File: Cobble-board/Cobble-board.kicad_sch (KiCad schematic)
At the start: 5 parts

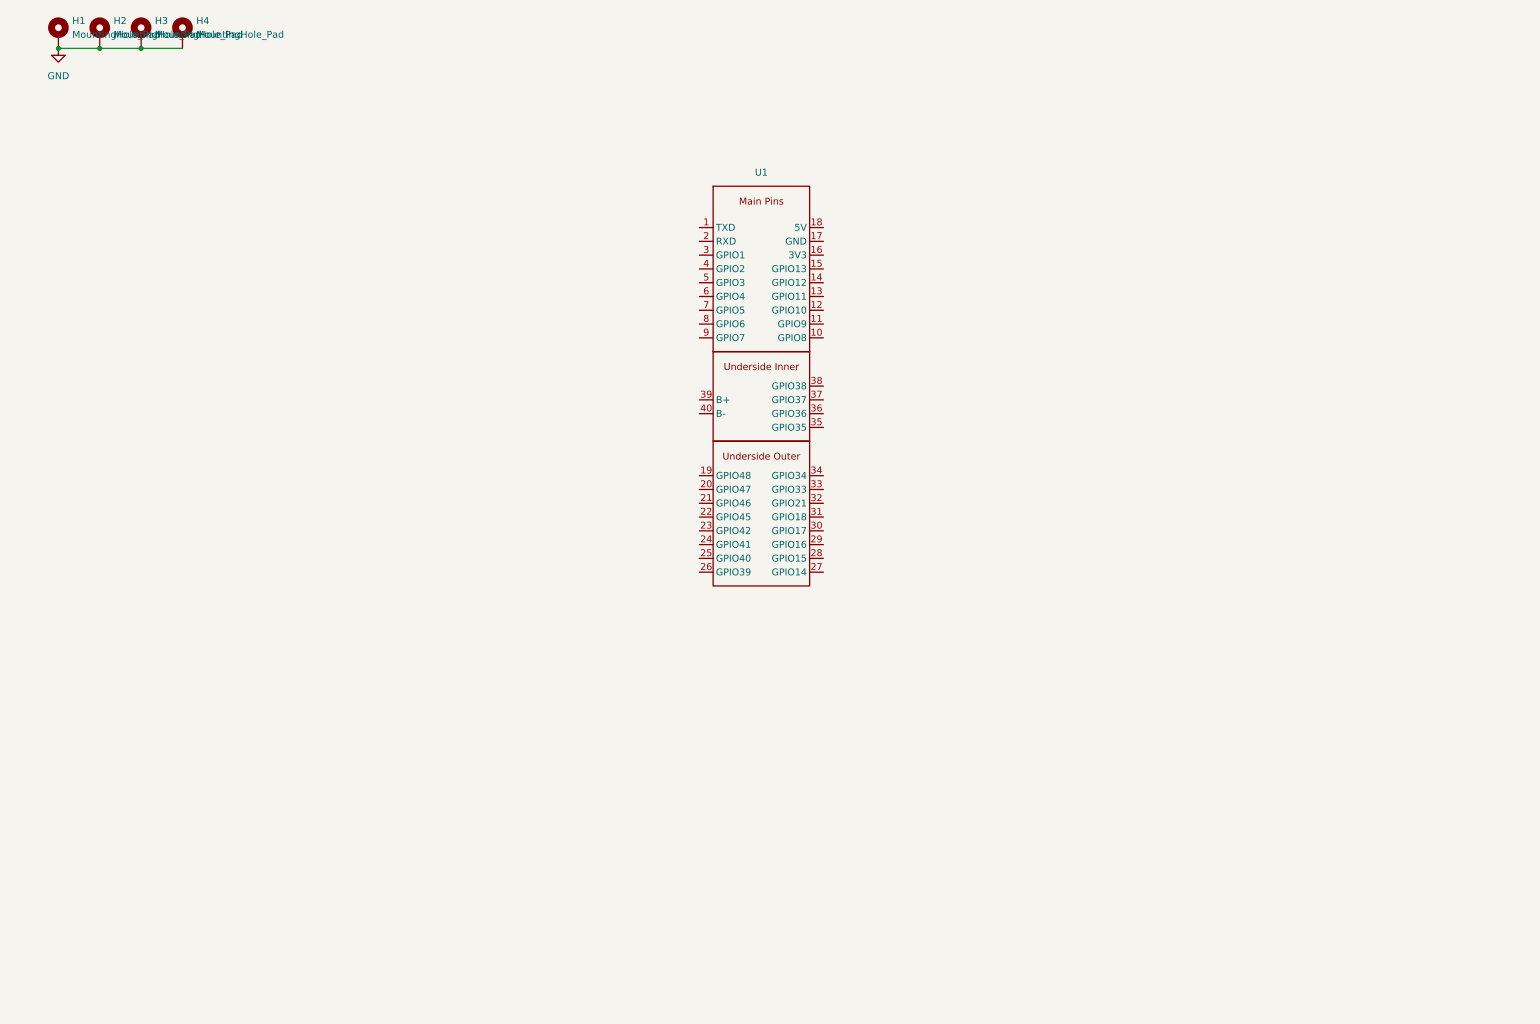
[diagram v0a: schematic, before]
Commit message: added most components.  waiting on clarification for speaker and i2c connectors
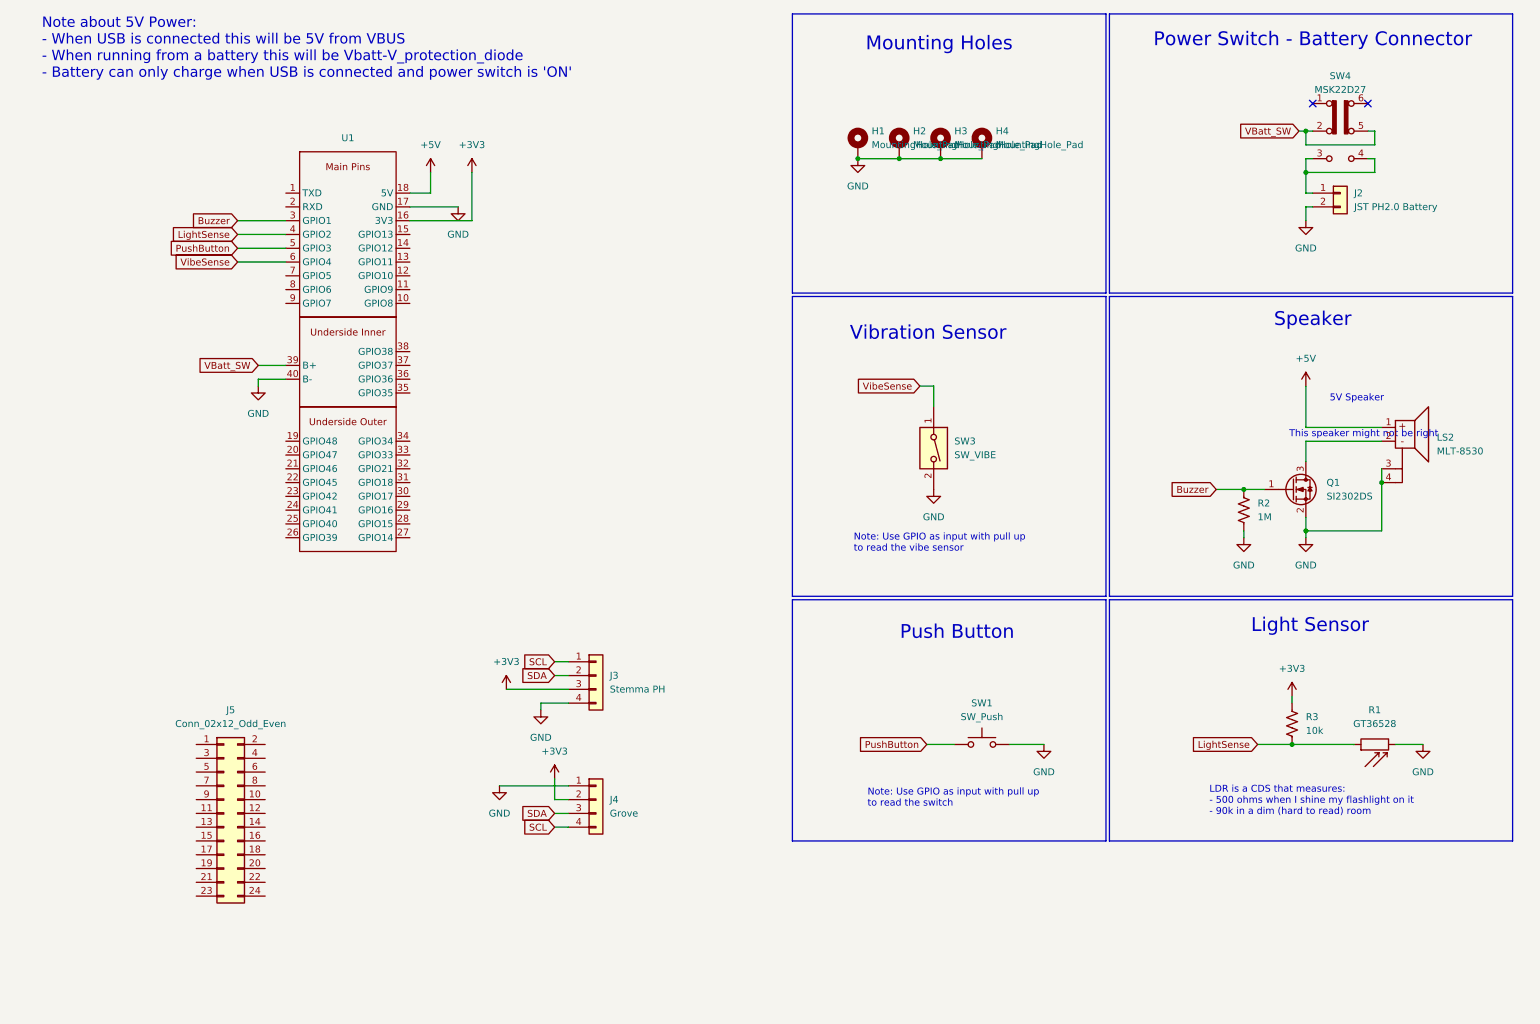
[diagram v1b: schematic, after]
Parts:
- added J2: JST PH2.0 Battery, Connector_JST:JST_PH_S2B-PH-K_1x02_P2.00mm_Horizontal, symbol Connector_Generic:Conn_01x02
- added J3: Stemma PH, Connector_JST:JST_PH_S4B-PH-K_1x04_P2.00mm_Horizontal, symbol Connector_Generic:Conn_01x04
- added J4: Grove, Connector_JST:JST_PH_S4B-PH-K_1x04_P2.00mm_Horizontal, symbol Connector_Generic:Conn_01x04
- added J5: Conn_02x12_Odd_Even, Connector_PinHeader_2.54mm:PinHeader_2x12_P2.54mm_Vertical_SMD, symbol Connector_Generic:Conn_02x12_Odd_Even
- added LS2: MLT-8530, Cobble_Library:MLT-8530, symbol Cobble_Library:MLT-8530
- added Q1: SI2302DS, Package_TO_SOT_SMD:SOT-23_Handsoldering, symbol Transistor_FET:Q_NMOS_GSD
- added R1: GT36528, Cobble_Library:GT36528, symbol Sensor_Optical:A1050
- added R2: 1M, Resistor_SMD:R_0603_1608Metric_Pad0.98x0.95mm_HandSolder, symbol Device:R_US
- added R3: 10k, Resistor_SMD:R_0603_1608Metric_Pad0.98x0.95mm_HandSolder, symbol Device:R_US
- added SW1: SW_Push, Button_Switch_SMD:SW_Push_1P1T_NO_CK_KSC6xxG, symbol Switch:SW_Push
- added SW3: SW_VIBE, Cobble_Library:X160, symbol Switch:SW_DIP_x01
- added SW4: MSK22D27, Cobble_Library:MSK22D27, symbol Switch:SW_Slide_DPDT
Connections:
- net GND: now also U1.17 (GND), U1.40 (B-), J2.2 (Pin_2), J3.4 (Pin_4), J4.1 (Pin_1), LS2.3 (Dummy), LS2.4 (Dummy), Q1.2 (S), R1.2, R2.2, SW1.2, SW3.2
- net +3V3: now reaches U1.16 (3V3)
- net +3V3: now also J3.3 (Pin_3), J4.2 (Pin_2), R3.1
- net +5V: now reaches U1.18 (5V)
- net +5V: now also LS2.1
- net Buzzer: now reaches U1.3 (GPIO1)
- net Buzzer: now also Q1.1 (G), R2.1
- net VBatt_SW: now reaches U1.39 (B+)
- net VBatt_SW: now also SW4.2 (B), SW4.5 (B)
- net LightSense: now reaches U1.4 (GPIO2)
- net LightSense: now also R1.1, R3.2
- net PushButton: now reaches U1.5 (GPIO3)
- net PushButton: now also SW1.1
- net VibeSense: now reaches U1.6 (GPIO4)
- net VibeSense: now also SW3.1
- new net: J2.1 (Pin_1), SW4.3 (C), SW4.4 (A)
- new net: LS2.2, Q1.3 (D)
- new net SCL: J3.1 (Pin_1), J4.4 (Pin_4)
- new net SDA: J3.2 (Pin_2), J4.3 (Pin_3)
- no-connect marks 0 -> 2
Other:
- note added: "5V Speaker"
- note added: "LDR is a CDS that measures: - 500 ohms when I shine my flashlight on it - 90k in a dim (hard to read) room"
- note added: "Light Sensor"
- note added: "Mounting Holes"
- note added: "Note about 5V Power: - When USB is connected this will be 5V from VBUS - When running from a battery this will be Vbatt-V_protection_diode - Battery can only charge when USB is connected and power switch is 'ON'"
- note added: "Note: Use GPIO as input with pull up to read the switch"
- note added: "Note: Use GPIO as input with pull up to read the vibe sensor"
- note added: "Power Switch - Battery Connector"
- note added: "Push Button"
- note added: "Speaker"
- note added: "This speaker might not be right"
- note added: "Vibration Sensor"
- moved on the sheet: H1, H2, H3, H4, U1

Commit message: main PWB is nearly complete.  need to add logo and fix one rat line.  added a cobble-board-test for a simpler single sided fab test board
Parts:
- J2: footprint Connector_JST:JST_PH_S2B-PH-K_1x02_P2.00mm_Horizontal -> Cobble_Library:Battery_1x02_P2.00mm_Horizontal
- J3, J4: footprint Connector_JST:JST_PH_S4B-PH-K_1x04_P2.00mm_Horizontal -> Cobble_Library:Stemma_Grove_1x04_P2.00mm_Horizontal
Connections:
- net +3V3: now also J5.10 (Pin_10), J5.15 (Pin_15), J5.16 (Pin_16), J5.21 (Pin_21), J5.4 (Pin_4), J5.9 (Pin_9)
- net +5V: now also J5.3 (Pin_3)
- net Buzzer: now also U1.10 (GPIO8); no longer U1.3 (GPIO1)
- net GND: now also J5.1 (Pin_1), J5.13 (Pin_13), J5.14 (Pin_14), J5.19 (Pin_19), J5.2 (Pin_2), J5.7 (Pin_7), J5.8 (Pin_8)
- net LightSense: now also U1.26 (GPIO39); no longer U1.4 (GPIO2)
- net SCL: now also U1.8 (GPIO6)
- net SDA: now also U1.9 (GPIO7)
- net VBatt_SW: now also SW4.1 (A)
- net VibeSense: now also U1.25 (GPIO40); no longer U1.6 (GPIO4)
- net TXD-GPIO43: now reaches U1.1 (TXD)
- net TXD-GPIO43: now also J5.24 (Pin_24)
- net GPIO9: now reaches U1.11 (GPIO9)
- net GPIO9: now also J5.12 (Pin_12)
- net GPIO10: now reaches U1.12 (GPIO10)
- net GPIO10: now also J5.18 (Pin_18)
- net GPIO11: now reaches U1.13 (GPIO11)
- net GPIO11: now also J5.20 (Pin_20)
- net GPIO12: now reaches U1.14 (GPIO12)
- net GPIO12: now also J5.23 (Pin_23)
- net GPIO13: now reaches U1.15 (GPIO13)
- net RXD-GPIO44: now reaches U1.2 (RXD)
- net RXD-GPIO44: now also J5.22 (Pin_22)
- net GPIO5: now reaches U1.7 (GPIO5)
- net GPIO5: now also J5.6 (Pin_6)
- net GPIO2: now reaches J5.11 (Pin_11)
- net GPIO2: now also U1.4 (GPIO2)
- net GPIO1: now reaches J5.17 (Pin_17)
- net GPIO1: now also U1.3 (GPIO1)
- net GPIO4: now reaches J5.5 (Pin_5)
- net GPIO4: now also U1.6 (GPIO4)
- no-connect marks 2 -> 20
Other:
- note added: "Note: This battery connector pinout seems to match standard adafruit batteries"

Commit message: Cobbl-board-test is complete and tested
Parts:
- R3: value 10k -> 100k
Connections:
- net RXD-GPIO44: no longer J5.22 (Pin_22)
- net TXD-GPIO43: no longer J5.24 (Pin_24)
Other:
- note added: "get atleast 4 pins to be ADC on header Group 4 pins to SPI"
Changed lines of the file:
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@@
 		)
 	)
+	(text "get atleast 4 pins to be ADC on header\nGroup 4 pins to SPI"
+		(exclude_from_sim no)
+		(at 70.104 134.874 0)
+		(effects
+			(font
+				(size 1.27 1.27)
+			)
+		)
+	)
 	(text "Note: This battery connector pinout \nseems to match standard adafruit batteries"
 		(exclude_from_sim no)
@@
 	(global_label "TXD-GPIO43"
 		(shape input)
-		(at 59.69 175.26 0)
-		(fields_autoplaced yes)
-		(effects
-			(font
-				(size 1.27 1.27)
-			)
-			(justify left)
-		)
-		(property "Intersheetrefs" "${INTERSHEET_REFS}"
-			(at 74.589 175.26 0)
-			(hide yes)
-			(show_name no)
-			(do_not_autoplace no)
-			(effects
-				(font
-					(size 1.27 1.27)
-				)
-				(justify left)
-			)
-		)
-	)
-	(global_label "TXD-GPIO43"
-		(shape input)
 		(at 49.53 45.72 180)
 		(fields_autoplaced yes)
@@
 		)
 	)
-	(global_label "RXD-GPIO44"
-		(shape input)
-		(at 59.69 172.72 0)
-		(fields_autoplaced yes)
-		(effects
-			(font
-				(size 1.27 1.27)
-			)
-			(justify left)
-		)
-		(property "Intersheetrefs" "${INTERSHEET_REFS}"
-			(at 74.8914 172.72 0)
-			(hide yes)
-			(show_name no)
-			(do_not_autoplace no)
-			(effects
-				(font
-					(size 1.27 1.27)
-				)
-				(justify left)
-			)
-		)
-	)
 	(global_label "LightSense"
 		(shape input)
@@
 			)
 		)
-		(property "Value" "10k"
+		(property "Value" "100k"
 			(at 246.38 144.7799 0)
 			(show_name no)

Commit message: Cobble schematic is updated with changes identified from Cobble-board-test. issues fixed: vibe sensor pad too small, SW1 pin spacing wrong, light sensor wired to non-ADC pin, 4 spins on ADC header for SPI, missing I2C pullup resistors, light sensor R shoudl be smaller (10K), SW4 alignment holes too small, ESP32S3 footprint didn't have battery charge boost pads
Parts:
- added R4, R5: 4k7, Resistor_SMD:R_0603_1608Metric_Pad0.98x0.95mm_HandSolder, symbol Device:R_US
- R3: value 100k -> 10k
- SW1: footprint Button_Switch_SMD:SW_Push_1P1T_NO_CK_KSC6xxG -> Cobble_Library:SW_Push_1P1T
- U1: footprint Cobble_Library:ESP32S3-supermini -> Cobble_Library:ESP32S3-supermini-v2
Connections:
- net +3V3: now also R4.2, R5.2
- net GPIO1: now also J5.11 (Pin_11); no longer J5.17 (Pin_17)
- net GPIO10: now also J5.24 (Pin_24); no longer J5.18 (Pin_18)
- net GPIO11: now also J5.22 (Pin_22); no longer J5.20 (Pin_20)
- net GPIO12: now also J5.20 (Pin_20); no longer J5.23 (Pin_23)
- net GPIO13: now also J5.18 (Pin_18)
- net GPIO2: now also J5.17 (Pin_17); no longer J5.11 (Pin_11)
- net GPIO4: now also J5.23 (Pin_23); no longer J5.5 (Pin_5)
- net GPIO5: no longer J5.6 (Pin_6), U1.7 (GPIO5)
- net LightSense: now also U1.7 (GPIO5); no longer U1.26 (GPIO39)
- net RXD-GPIO44: now also J5.6 (Pin_6)
- net SCL: now also R4.1
- net SDA: now also R5.1
- net TXD-GPIO43: now also J5.5 (Pin_5)
- new net: U1.41 (ChrgBst), U1.42 (ChrgBst)
- no-connect marks 20 -> 19
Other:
- note added: "Note about 5V Power: - When USB is connected this will be 5V from VBUS - When running from a battery this will be Vbatt-V_protection_diode - Battery can only charge when USB is connected and power switch is 'ON' Note about ADC/GPIO: - GPIO1 to 10 are available as ADC0 to 9"
- note removed: "Note about 5V Power: - When USB is connected this will be 5V from VBUS - When running from a battery this will be Vbatt-V_protection_diode - Battery can only charge when USB is connected and power switch is 'ON'"

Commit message: schemtic updated for ESP32-C6 board, but we have decided not to use that version due to usability issues
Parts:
- removed U1: (no value), Cobble_Library:ESP32S3-supermini-v2, symbol Cobble_Library:ESP32S2-supermini
- added U1: (no value), RF_Module:ESP32-C3-WROOM-02, symbol Cobble_Library:ESP32C3-supermini
- J2: footprint Cobble_Library:Battery_1x02_P2.00mm_Horizontal -> Connector_JST:JST_PH_B2B-PH-SM4-TB_1x02-1MP_P2.00mm_Vertical
- J3: footprint Cobble_Library:Stemma_Grove_1x04_P2.00mm_Horizontal -> Connector_JST:JST_PH_B4B-PH-SM4-TB_1x04-1MP_P2.00mm_Vertical
- J4: footprint Cobble_Library:Stemma_Grove_1x04_P2.00mm_Horizontal -> Grove:GROVE-HW4-SMD-2.0
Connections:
- net GPIO4 is gone; now on net GPIO2: J5.23 (Pin_23)
- net +3V3: now also U1.18 (3V3)
- net +5V: now also U1.20 (5V)
- net Buzzer: now also U1.10 (GPIO7)
- net GND: now also U1.19 (GND), U1.27 (B-)
- net GPIO1: now also J5.17 (Pin_17), U1.4 (GPIO1); no longer J5.11 (Pin_11)
- net GPIO2: now also U1.5 (GPIO2); no longer J5.17 (Pin_17)
- net LightSense: now also U1.9 (GPIO6)
- net PushButton: now also U1.12 (GPIO9)
- net SCL: now also U1.15 (GPIO18)
- net SDA: now also U1.16 (GPIO19)
- net VBatt_SW: now also U1.26 (B+)
- net VibeSense: now also U1.13 (GPIO14)
- net GPIO10 renamed GPIO20
- net GPIO20: now also U1.17 (GPIO120)
- net GPIO11 renamed GPIO21
- net GPIO21: now also U1.25 (GPIO21)
- net GPIO12 renamed GPIO22
- net GPIO22: now also U1.24 (GPIO22)
- net GPIO13 renamed GPIO23
- net GPIO23: now also U1.21 (GPIO23)
- net GPIO9 renamed GPIO3
- net GPIO3: now also U1.6 (GPIO3)
- net RXD-GPIO44 renamed RXD
- net RXD: now also U1.2 (RXD|GPIO17)
- net TXD-GPIO43 renamed TXD
- net TXD: now also U1.1 (TXD|GPIO16)
- new net GPIO0: J5.11 (Pin_11), U1.3 (GPIO0)
- no-connect marks 19 -> 7
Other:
- note added: "GPIO Header"
- note added: "I2C Connectors"
- note added: "Note about 5V Power: - When USB is connected this will be 5V from VBUS - When running from a battery this will be Vbatt-V_protection_diode - Battery can only charge when USB is connected and power switch is 'ON' Notes about GPIOs: - ADC: GPIO0 to 6 are available as ADC0 to 6 - USB D+/- are GPIO12, 13. JUST DON"T USE THEM! - Boot is GPIO9. Will share with onboard button."
- note removed: "Note about 5V Power: - When USB is connected this will be 5V from VBUS - When running from a battery this will be Vbatt-V_protection_diode - Battery can only charge when USB is connected and power switch is 'ON' Note about ADC/GPIO: - GPIO1 to 10 are available as ADC0 to 9"
- note removed: "get atleast 4 pins to be ADC on header Group 4 pins to SPI"
- moved on the sheet: J3, J4, J5, R4, R5

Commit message: Cobble board is rev 1 is ready for review
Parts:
- removed U1: (no value), RF_Module:ESP32-C3-WROOM-02, symbol Cobble_Library:ESP32C3-supermini
- added U1: (no value), Cobble_Library:ESP32S3-supermini-v2, symbol Cobble_Library:ESP32S2-supermini
- R4, R5: now not fitted
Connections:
- net GPIO0 is gone; now on net GPIO2: J5.11 (Pin_11)
- net +3V3: now also U1.16 (3V3)
- net +5V: now also U1.18 (5V)
- net Buzzer: now also U1.10 (GPIO8)
- net GND: now also U1.17 (GND), U1.40 (B-)
- net GPIO1: now also J5.5 (Pin_5), U1.3 (GPIO1); no longer J5.17 (Pin_17)
- net GPIO2: now also U1.4 (GPIO2); no longer J5.23 (Pin_23)
- net LightSense: now also U1.9 (GPIO7)
- net PushButton: now also U1.35 (GPIO35)
- net RXD: now also U1.2 (RXD); no longer J5.6 (Pin_6)
- net SCL: now also U1.29 (GPIO16)
- net SDA: now also U1.30 (GPIO17)
- net TXD: now also U1.1 (TXD); no longer J5.5 (Pin_5)
- net VBatt_SW: now also U1.39 (B+)
- net VibeSense: now also U1.11 (GPIO9)
- net GPIO20 renamed GPIO13
- net GPIO13: now also U1.15 (GPIO13)
- net GPIO21 renamed GPIO12
- net GPIO12: now also U1.14 (GPIO12)
- net GPIO22 renamed GPIO11
- net GPIO11: now also U1.13 (GPIO11)
- net GPIO23 renamed GPIO10
- net GPIO10: now also U1.12 (GPIO10)
- net GPIO3 renamed GPIO15
- net GPIO15: now also U1.28 (GPIO15)
- new net: U1.41 (ChrgBst), U1.42 (ChrgBst)
- new net GPIO4: J5.17 (Pin_17), U1.6 (GPIO4)
- new net GPIO5: J5.23 (Pin_23), U1.7 (GPIO5)
- new net GPIO6: J5.6 (Pin_6), U1.8 (GPIO6)
- no-connect marks 7 -> 17
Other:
- note added: "Note about 5V Power: - When USB is connected this will be 5V from VBUS - When running from a battery this will be Vbatt-V_protection_diode - Battery can only charge when USB is connected and power switch is 'ON' Notes about GPIOs: - ADC: GPIO1 to 10 are available as ADC0 to 9 - GPIO3 is overloaded with JTAG src - GPIO45, 46 are bootstrapping pins"
- note removed: "Note about 5V Power: - When USB is connected this will be 5V from VBUS - When running from a battery this will be Vbatt-V_protection_diode - Battery can only charge when USB is connected and power switch is 'ON' Notes about GPIOs: - ADC: GPIO0 to 6 are available as ADC0 to 6 - USB D+/- are GPIO12, 13. JUST DON"T USE THEM! - Boot is GPIO9. Will share with onboard button."
- note removed: "This speaker might not be right"
- company: WildCircuits | Tinkerfarm | Brockport Original Builds -> Tinkerfarm | WildCircuits | Brockport Original Builds
- moved on the sheet: J3, J4, J5
